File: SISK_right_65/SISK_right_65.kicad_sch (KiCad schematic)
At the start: 87 parts, among them J1 OLED_128x32, J2 Battery Conn, J3 alternative on/off SW (wired), SW1 "6", SW10 "Z", SW11 "U", SW12 "I", SW13 "O", SW14 "P", SW15 "Ü", SW16 "*", SW17 "Enter", SW18 "Del", SW19 "H", SW2 "7", SW20 "J", SW21 "K", SW22 "L", SW23 "Ö", SW24 "Ä", SW25 "'", SW26 "PGUP", SW27 "N", SW28 "M", SW29 ";", SW3 "8", SW30 ":", SW31 "-", SW32 "shift_R", SW33 "UP", SW34 "PGDOWN", SW35 "SPACE_R", SW36 "Alt", SW37 FN, SW38 "Ctrl", SW39 "Left", SW4 "9", SW40 "Down", SW41 "Right", SW5 "0", SW6 "ß", SW7 "`", SW8 "Backspace", SW9 "^", U1 Nice_Nano_V2

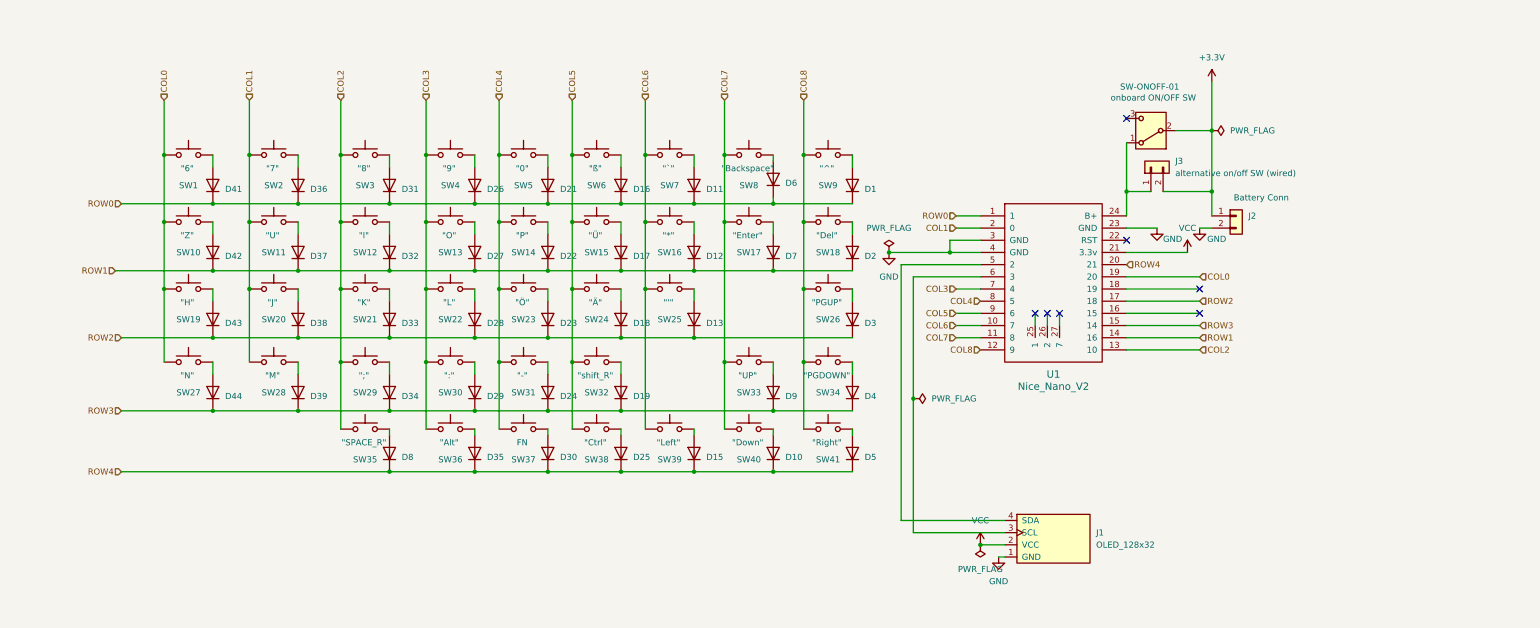
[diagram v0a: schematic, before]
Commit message: fixed schematics, added optional pullup resistors
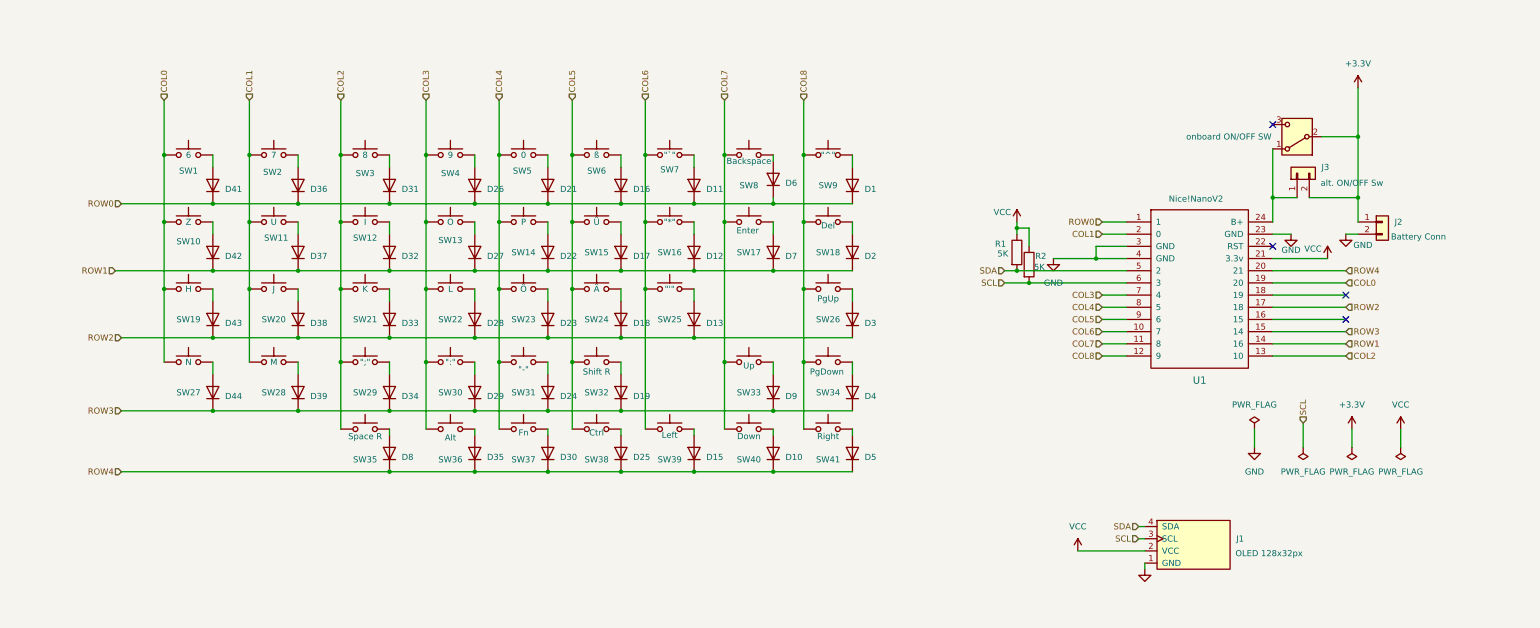
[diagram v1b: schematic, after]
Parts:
- added R1, R2: 5K, Resistor_SMD:R_1206_3216Metric_Pad1.30x1.75mm_HandSolder, symbol Device:R
- J1: Label (none) -> OLED 128x32px
- J2: value Battery Conn -> Conn; Label (none) -> Battery Conn
- J3: value alternative on/off SW (wired) -> SWITCH; Label (none) -> alt. ON/OFF Sw
- SW-ONOFF-01: value onboard ON/OFF SW -> ~; Label (none) -> onboard ON/OFF SW
- SW1: value "6" -> SW_push; Label (none) -> 6
- SW10: value "Z" -> SW_push; Label (none) -> Z
- SW11: value "U" -> SW_push; Label (none) -> U
- SW12: value "I" -> SW_push; Label (none) -> I
- SW13: value "O" -> SW_push; Label (none) -> O
- SW14: value "P" -> SW_push; Label (none) -> P
- SW15: value "Ü" -> SW_push; Label (none) -> Ü
- SW16: value "*" -> SW_push; Label (none) -> "*"
- SW17: value "Enter" -> SW_push; Label (none) -> Enter
- SW18: value "Del" -> SW_push; Label (none) -> Del
- SW19: value "H" -> SW_push; Label (none) -> H
- SW2: value "7" -> SW_push; Label (none) -> 7
- SW20: value "J" -> SW_push; Label (none) -> J
- SW21: value "K" -> SW_push; Label (none) -> K
- SW22: value "L" -> SW_push; Label (none) -> L
- SW23: value "Ö" -> SW_push; Label (none) -> Ö
- SW24: value "Ä" -> SW_push; Label (none) -> Ä
- SW25: value "'" -> SW_push; Label (none) -> "'"
- SW26: value "PGUP" -> SW_push; Label (none) -> PgUp
- SW27: value "N" -> SW_push; Label (none) -> N
- SW28: value "M" -> SW_push; Label (none) -> M
- SW29: value ";" -> SW_push; Label (none) -> ";"
- SW3: value "8" -> SW_push; Label (none) -> 8
- SW30: value ":" -> SW_push; Label (none) -> ":"
- SW31: value "-" -> SW_push; Label (none) -> "-"
- SW32: value "shift_R" -> SW_push; Label (none) -> Shift R
- SW33: value "UP" -> SW_push; Label (none) -> Up
- SW34: value "PGDOWN" -> SW_push; Label (none) -> PgDown
- SW35: value "SPACE_R" -> SW_push; Label (none) -> Space R
- SW36: value "Alt" -> SW_push; Label (none) -> Alt
- SW37: value FN -> SW_push; Label (none) -> Fn
- SW38: value "Ctrl" -> SW_push; Label (none) -> Ctrl
- SW39: value "Left" -> SW_push; Label (none) -> Left
- SW4: value "9" -> SW_push; Label (none) -> 9
- SW40: value "Down" -> SW_push; Label (none) -> Down
- SW41: value "Right" -> SW_push; Label (none) -> Right
- SW5: value "0" -> SW_push; Label (none) -> 0
- SW6: value "ß" -> SW_push; Label (none) -> ß
- SW7: value "`" -> SW_push; Label (none) -> "`"
- SW8: value "Backspace" -> SW_push; Label (none) -> Backspace
- SW9: value "^" -> SW_push; Label (none) -> "^"
- U1: Label (none) -> Nice!NanoV2
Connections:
- net VCC: now also R1.1, R2.1
- net SCL: now reaches J1.3 (SCL), U1.6 (3)
- net SCL: now also R2.2
- net SDA: now reaches J1.4 (SDA), U1.5 (2)
- net SDA: now also R1.2
- no-connect marks 7 -> 4
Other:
- moved on the sheet: J1, J2, J3

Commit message: fixed most of issues, updated 60% version
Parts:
- D1, D10, D11, D12, D13, D15, D16, D17, D18, D19, D2, D21, D22, D23, D24, D25, D26, D27, D28, D29, D3, D30, D31, D32, D33, D34, D35, D36, D37, D38, D39, D4, D41, D42, D43, D44, D5, D6, D7, D8, D9: MPN (none) -> 1N4148W
- J1: MPN (none) -> OLED 128x32 i2C
- J2: MPN (none) -> S2B-PH-K-S(LF)(SN)
- J3: MPN (none) -> not known yet
- R1, R2: MPN (none) -> RC1206JR-072K2L
- SW-ONOFF-01: MPN (none) -> MSK12C01
- SW1, SW10, SW11, SW12, SW13, SW14, SW15, SW16, SW17, SW18, SW19, SW2, SW20, SW21, SW22, SW23, SW24, SW25, SW26, SW27, SW28, SW29, SW3, SW30, SW31, SW32, SW33, SW34, SW35, SW36, SW37, SW38, SW39, SW4, SW40, SW41, SW5, SW6, SW7, SW8, SW9: MPN (none) -> CPG151101S11
- U1: MPN (none) -> nice!nano v2 or compatible
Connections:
- net +VDC: now reaches J3.1 (Pin_1), SW-ONOFF-01.1 (A), U1.24 (B+)
- net +3.3V renamed +BATT
- net VCC renamed +3,3V
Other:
- moved on the sheet: J2, J3

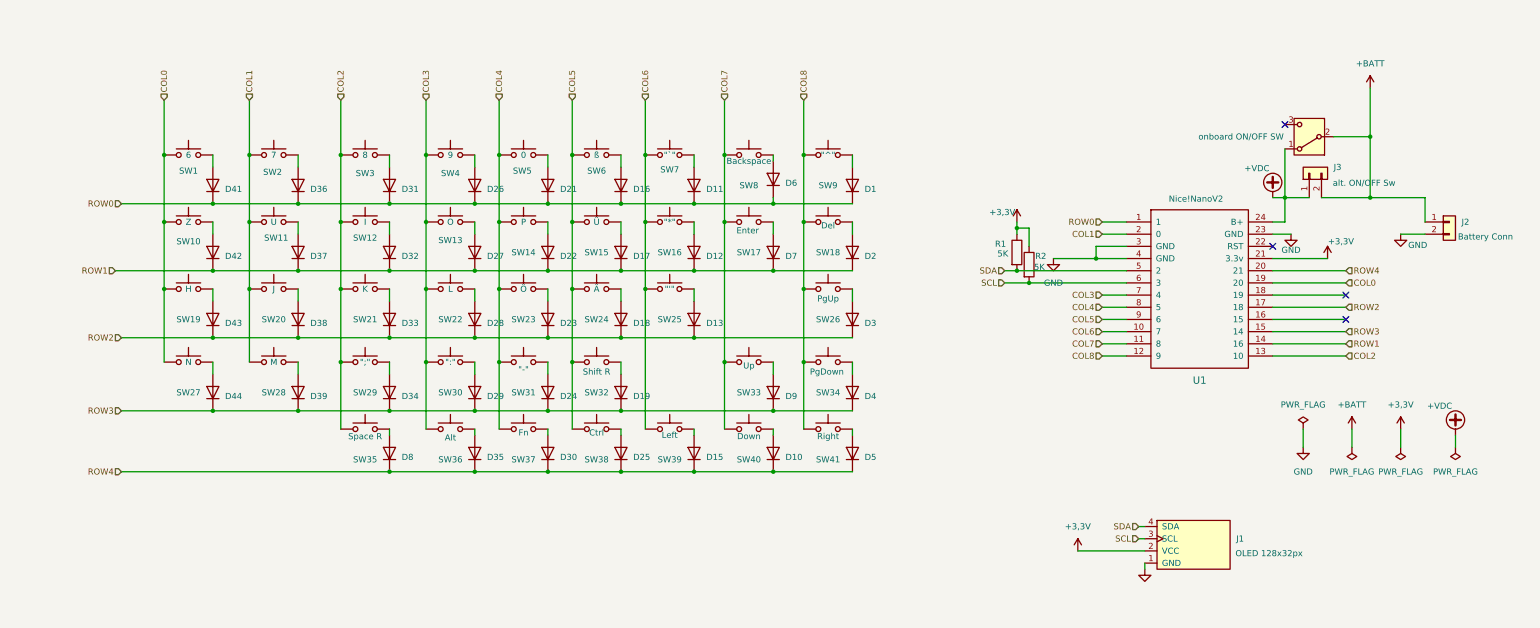
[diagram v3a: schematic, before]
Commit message: improved the whole mounting hole situation
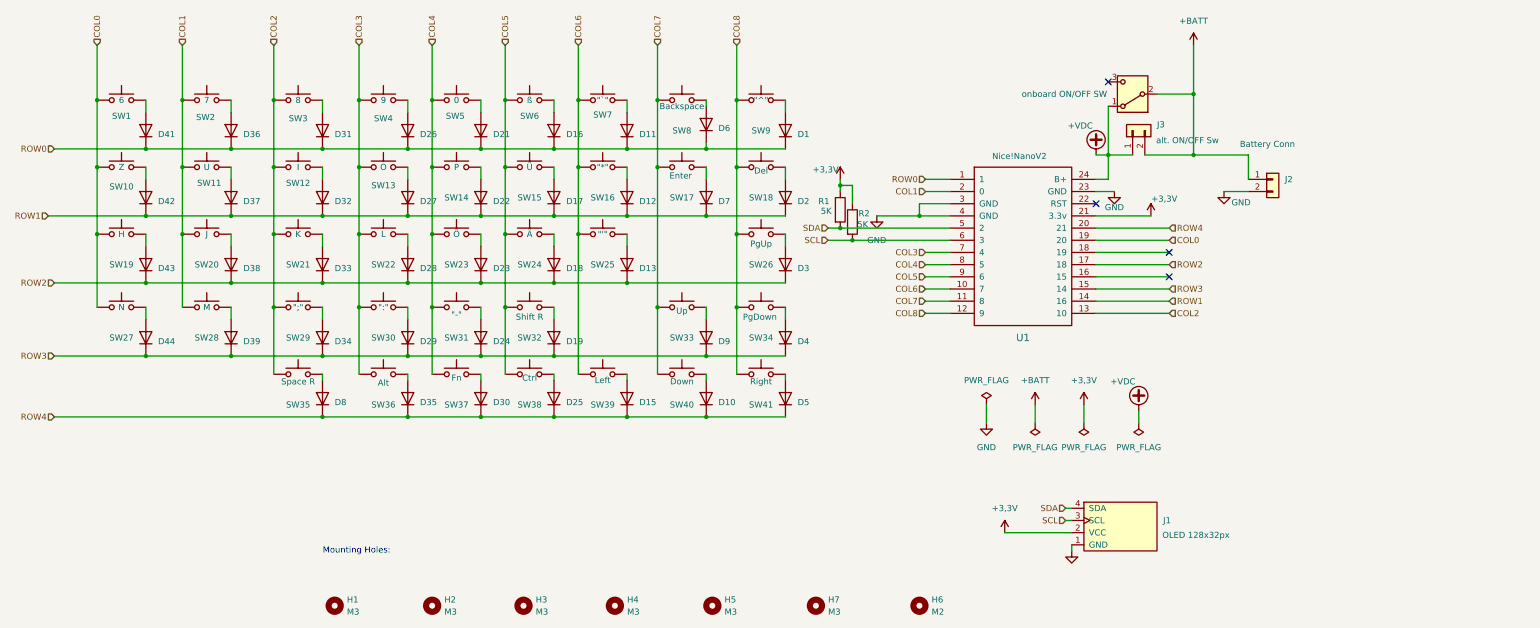
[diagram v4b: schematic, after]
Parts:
- added H1, H2, H3, H4, H5, H7: M3, MountingHole:MountingHole_3.2mm_M3_ISO7380_Pad_TopBottom, symbol Mechanical:MountingHole
- added H6: M2, MountingHole:MountingHole_2.2mm_M2_ISO7380_Pad_TopOnly, symbol Mechanical:MountingHole
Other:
- note added: "Mounting Holes:"
- moved on the sheet: D1, D10, D11, D12, D13, D15, D16, D17, D18, D19, D2, D21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

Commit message: last changes on silkscreen before manufaturing
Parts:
- J2: value Conn -> Batt
- SW37: Label Fn -> Super
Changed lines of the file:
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@@
 			)
 		)
-		(property "Label" "Fn"
-			(at 107.95 92.71 0)
+		(property "Label" "Super"
+			(at 107.95 93.98 0)
 			(effects
 				(font
@@
 			)
 		)
-		(property "Value" "Conn"
+		(property "Value" "Batt"
 			(at 277.622 48.26 0)
 			(effects
@@
 		)
 		(property "Label" "Ctrl"
-			(at 123.19 92.71 0)
-			(effects
-				(font
+			(at 123.19 93.726 0)
+			(effects
+				(font
